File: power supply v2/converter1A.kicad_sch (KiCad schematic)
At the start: 46 parts, among them IC1 LM25145RGYR, IC3 LMR50410YQDBVRQ1, J1 1.5 mm, J3 1933189, J4 Conn_01x04_Pin 1.27mm, Q1 35A, 30V, Q2 35A Id, 30V Vds

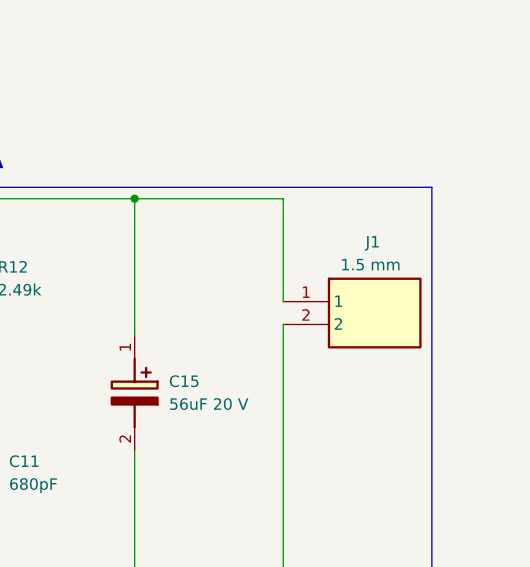
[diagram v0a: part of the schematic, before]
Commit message: add license
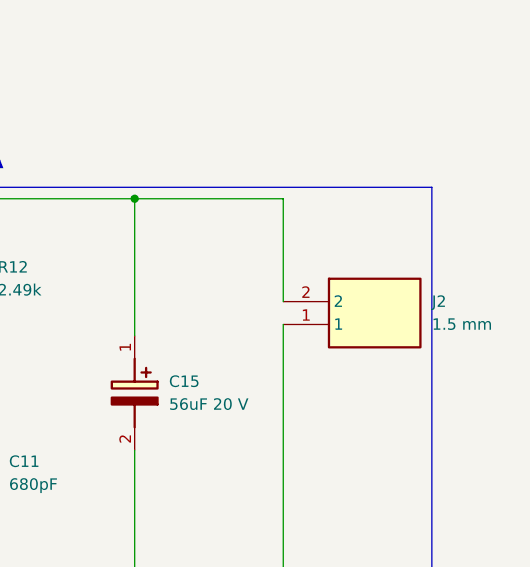
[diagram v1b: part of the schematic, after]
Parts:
- removed J1: 1.5 mm, 1933189, symbol 1933189:1933189
- added J2: 1.5 mm, 1933189, symbol 1933189:1933189
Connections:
- net GND: now also J2.1
- net at C15.1 (+), L1.2, R10.1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: now also J2.2
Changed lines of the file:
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@@
+	)
+	(symbol
+		(lib_name "1933189_1")
+		(lib_id "1933189:1933189")
+		(at 267.97 81.28 0)
+		(unit 1)
+		(exclude_from_sim no)
+		(in_bom yes)
+		(on_board yes)
+		(dnp no)
+		(fields_autoplaced yes)
+		(property "Reference" "J2"
+			(at 284.48 81.2799 0)
+			(effects
+				(font
+					(size 1.27 1.27)
+				)
+				(justify left)
+			)
+		)
+		(property "Value" "1.5 mm"
+			(at 284.48 83.8199 0)
+			(effects
+				(font
+					(size 1.27 1.27)
+				)
+				(justify left)
+			)
+		)
+		(property "Footprint" "1933189"
+			(at 284.48 176.2 0)
+			(effects
+				(font
+					(size 1.27 1.27)
+				)
+				(justify left top)
+				(hide yes)
+			)
+		)
+		(property "Datasheet" "http://www.phoenixcontact.com/de/produkte/1933189/pdf"
+			(at 284.48 276.2 0)
+			(effects
+				(font
+					(size 1.27 1.27)
+				)
+				(justify left top)
+				(hide yes)
+			)
+		)
+		(property "Description" "Pin strip, nominal cross section: 1.5 mm?, color: black, nominal current: 12 A (depends on the plug used), rated voltage (III/2): 320 V, contact surface: Tin, type of contact: Male connector, Number of potentials: 2, Number of rows: 1, Number of positions per row: 2, number of connections: 2, product range: PST 1,3/..-V, pitch: 5 mm, mounting: THR soldering, pin layout: Linear pinning, solder pin [P]: 3.5 mm, Stecksystem: COMBICON COMPACT PST 1,3, Locking: without, type of packaging: packed in cardboard, Th"
+			(at 267.97 81.28 0)
+			(effects
+				(font
+					(size 1.27 1.27)
+				)
+				(hide yes)
+			)
+		)
+		(property "Height" "9.5"
+			(at 284.48 476.2 0)
+			(effects
+				(font
+					(size 1.27 1.27)
+				)
+				(justify left top)
+				(hide yes)
+			)
+		)
+		(property "Mouser Part Number" "651-1933189"
+			(at 284.48 576.2 0)
+			(effects
+				(font
+					(size 1.27 1.27)
+				)
+				(justify left top)
+				(hide yes)
+			)
+		)
+		(property "Mouser Price/Stock" "https://www.mouser.co.uk/ProductDetail/Phoenix-Contact/1933189?qs=wdlOgCqRo4yJtNGn6%2FIahw%3D%3D"
+			(at 284.48 676.2 0)
+			(effects
+				(font
+					(size 1.27 1.27)
+				)
+				(justify left top)
+				(hide yes)
+			)
+		)
+		(property "Manufacturer_Name" "Phoenix Contact"
+			(at 284.48 776.2 0)
+			(effects
+				(font
+					(size 1.27 1.27)
+				)
+				(justify left top)
+				(hide yes)
+			)
+		)
+		(property "Manufacturer_Part_Number" "1933189"
+			(at 284.48 876.2 0)
+			(effects
+				(font
+					(size 1.27 1.27)
+				)
+				(justify left top)
+				(hide yes)
+			)
+		)
+		(pin "1"
+		)
+		(pin "2"
+		)
+		(instances
+			(project ""
+				(path "/227c4948-9b5e-42be-82b5-2619f1ed7477"
+					(reference "J2")
+					(unit 1)
+				)
+			)
+		)
 	)
 	(symbol
@@
 					(unit 1)
 				)
-			)
-		)
-	)
-	(symbol
-		(lib_id "1933189:1933189")
-		(at 267.97 81.28 0)
-		(unit 1)
-		(exclude_from_sim no)
-		(in_bom yes)
-		(on_board yes)
-		(dnp no)
-		(property "Reference" "J1"
-			(at 277.114 74.676 0)
-			(effects
-				(font
-					(size 1.27 1.27)
-				)
-				(justify left)
-			)
-		)
-		(property "Value" "1.5 mm"
-			(at 274.32 77.216 0)
-			(effects
-				(font
-					(size 1.27 1.27)
-				)
-				(justify left)
-			)
-		)
-		(property "Footprint" "1933189"
-			(at 284.48 176.2 0)
-			(effects
-				(font
-					(size 1.27 1.27)
-				)
-				(justify left top)
-				(hide yes)
-			)
-		)
-		(property "Datasheet" "http://www.phoenixcontact.com/de/produkte/1933189/pdf"
-			(at 284.48 276.2 0)
-			(effects
-				(font
-					(size 1.27 1.27)
-				)
-				(justify left top)
-				(hide yes)
-			)
-		)
-		(property "Description" "Pin strip, nominal cross section: 1.5 mm?, color: black, nominal current: 12 A (depends on the plug used), rated voltage (III/2): 320 V, contact surface: Tin, type of contact: Male connector, Number of potentials: 2, Number of rows: 1, Number of positions per row: 2, number of connections: 2, product range: PST 1,3/..-V, pitch: 5 mm, mounting: THR soldering, pin layout: Linear pinning, solder pin [P]: 3.5 mm, Stecksystem: COMBICON COMPACT PST 1,3, Locking: without, type of packaging: packed in cardboard, Th"
-			(at 267.97 81.28 0)
-			(effects
-				(font
-					(size 1.27 1.27)
-				)
-				(hide yes)
-			)
-		)
-		(property "Height" "9.5"
-			(at 284.48 476.2 0)
-			(effects
-				(font
-					(size 1.27 1.27)
-				)
-				(justify left top)
-				(hide yes)
-			)
-		)
-		(property "Mouser Part Number" "651-1933189"
-			(at 284.48 576.2 0)
-			(effects
-				(font
-					(size 1.27 1.27)
-				)
-				(justify left top)
-				(hide yes)
-			)
-		)
-		(property "Mouser Price/Stock" "https://www.mouser.co.uk/ProductDetail/Phoenix-Contact/1933189?qs=wdlOgCqRo4yJtNGn6%2FIahw%3D%3D"
-			(at 284.48 676.2 0)
-			(effects
-				(font
-					(size 1.27 1.27)
-				)
-				(justify left top)
-				(hide yes)
-			)
-		)
-		(property "Manufacturer_Name" "Phoenix Contact"
-			(at 284.48 776.2 0)
-			(effects
-				(font
-					(size 1.27 1.27)
-				)
-				(justify left top)
-				(hide yes)
-			)
-		)
-		(property "Manufacturer_Part_Number" "1933189"
-			(at 284.48 876.2 0)
-			(effects
-				(font
-					(size 1.27 1.27)
-				)
-				(justify left top)
-				(hide yes)
-			)
-		)
-		(pin "2"
-		)
-		(pin "1"
-		)
-		(instances
-			(project ""
-				(path "/227c4948-9b5e-42be-82b5-2619f1ed7477"
-					(reference "J1")
-					(unit 1)
-				)
